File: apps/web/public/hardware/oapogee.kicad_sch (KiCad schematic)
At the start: 44 parts, among them J1 USB4085-GF-A, J2 S2B-PH-K-S, J3 U.FL-R-SMT-1(10), J4 SWD-PADS, J5 U.FL-R-SMT-1(10), SW1 JS102011SCQN, SW2 B3U-1000P, SW3 B3U-1000P, U1 MCP73831, U2 TPS63001, U3 RP2350A, U4 W25Q128JVSIQ, U5 BMP390, U6 ICM-42688-P, U7 ADXL375, U8 SX1262, U9 MAX-M10S, Y1 ABM8-272-T3

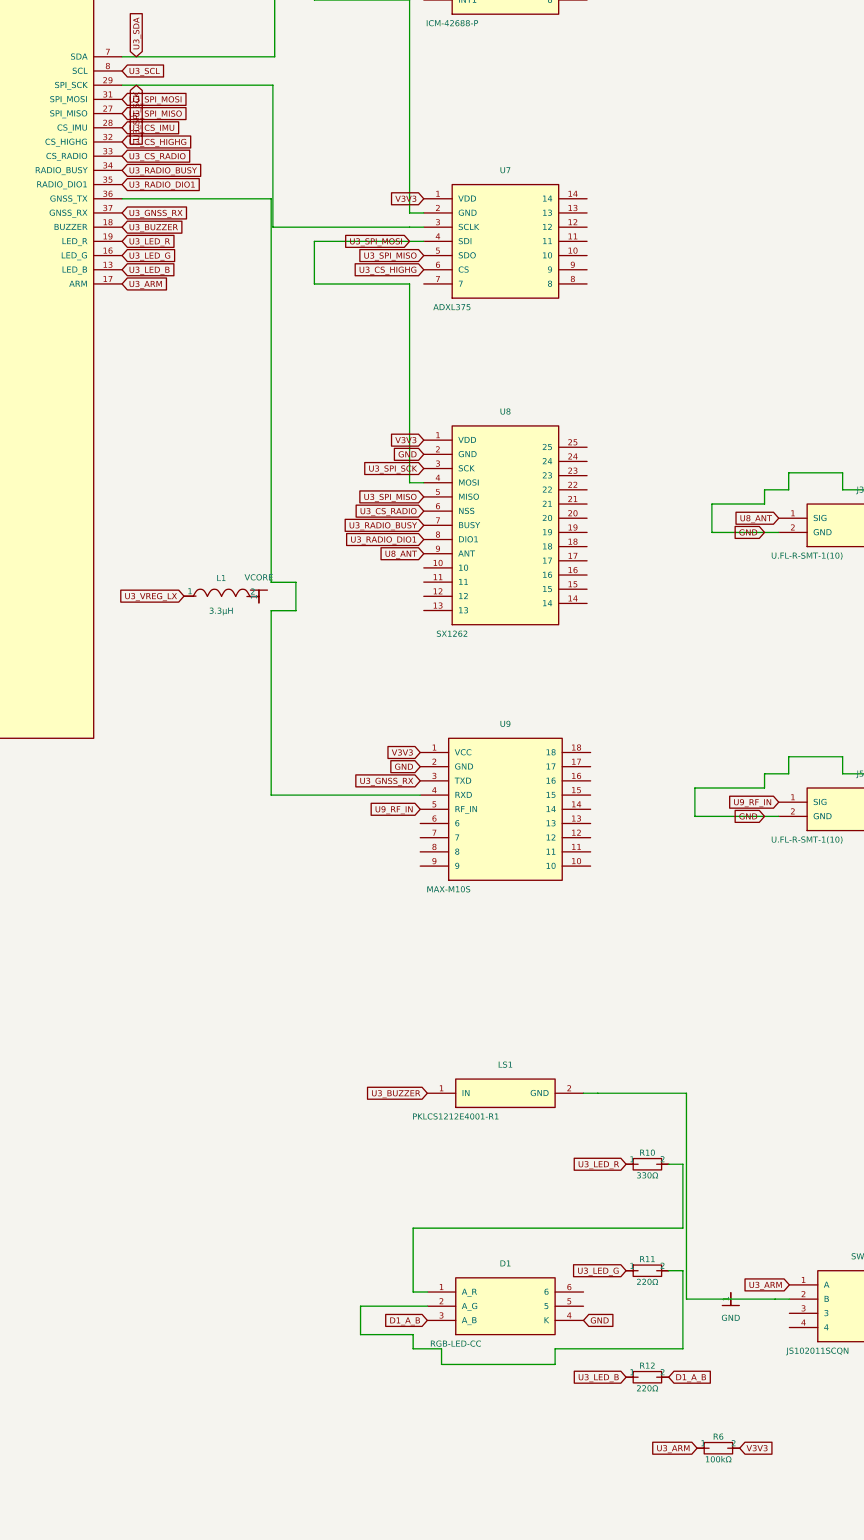
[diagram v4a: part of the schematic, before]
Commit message: Build the radio properly: the real SX1262 pinout, its crystal, its DC-DC
Semtech DS.SX1261-2.W.APP Table 2-1, transcribed for the QFN 4x4 24L and
cross-checked against revision 1.2 from 2019 and revision 2.2 from 2024. The
part had nine of twenty-five pins named. It has all of them now, and the four
supplies, four grounds, exposed pad, reset and DIO2 are wired.

Two parts the datasheet requires that this board did not have:

Y2, a 32 MHz crystal, because the radio has no reference without one. And it
gets no load capacitors, which looks like an omission next to the
microcontroller's crystal ten millimetres away and is not. Section 4.1.3: the
SX1262 "does not require the user to set external foot capacitors on the XTAL",
because it has programmable ones on XTA and XTB that cannot be switched off and
that the state machine sets to 19.7 pF on entering STDBY_XOSC. Adding external
capacitors would detune it.

L3, 15 uH between VREG and DCC_SW, which is what lets the radio use its
switching regulator instead of its linear one. Section 13.1.11 on not fitting
it: "Using only a linear regulator implies that the RX or TX current is almost
doubled." On a payload built around one small cell that is the largest single
number in the power budget.

The board is 92 mm rather than 78. Sixteen more connections in one corner put
the autorouter into a state where it was pushing vias to 0.028 mm from pads and
laying 114 pairs of copper that crossed each other, which is 114 shorts. More
length fixed it: 145 traces, no crossings, and the count of pairs too close for
the cheaper fabricator fell from 82 back to 40.

It is still 28 mm wide. Widening to 30 routed just as well and was wrong: the
sled has to slide into a 32.59 mm tube, so a 30 mm board leaves 1.3 mm a side
for a wall the sled prints at 1.2 mm. The router did not need the width.

What is still open, and it is one thing: the RF front end. The transmit output,
the receive inputs and the PA supply are still unconnected, because bet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
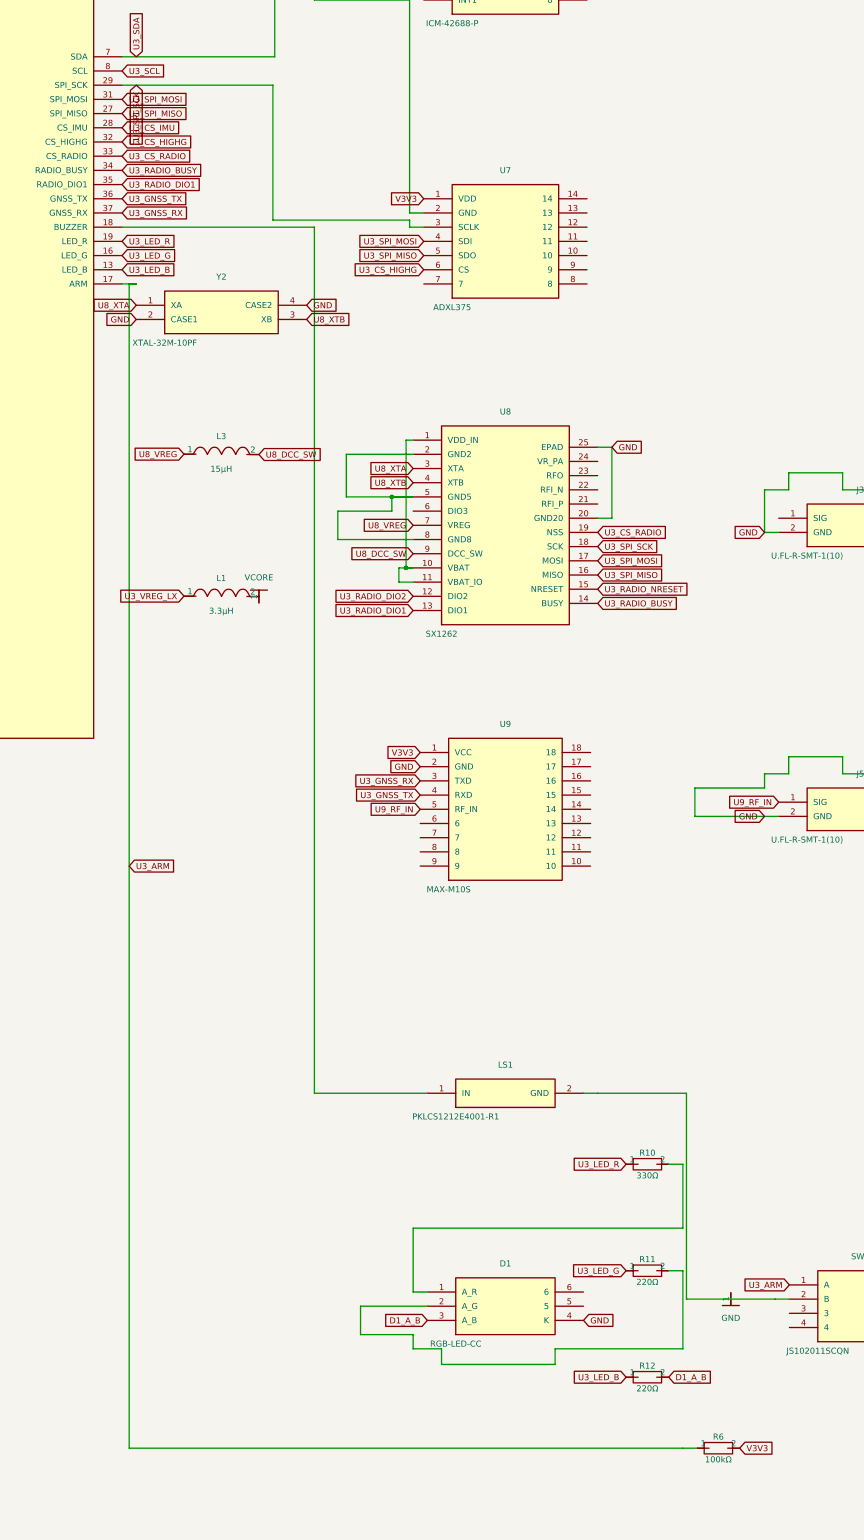
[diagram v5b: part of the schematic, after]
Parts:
- removed GND (x3): GND, symbol Custom:rail_down
- added GND (x3): GND, symbol Custom:rail_down
- added L3: 15µH, symbol Device:inductor_right
- added Y2: XTAL-32M-10PF, symbol Device:U_XTAL-32M-10PF
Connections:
- net GND: now also U8.20 (GND20), U8.25 (EPAD), Y2.2 (CASE1), Y2.4 (CASE2); no longer U8.2 (GND)
- net U3_CS_RADIO: now also U8.19 (NSS); no longer U8.6 (NSS)
- net U3_RADIO_BUSY: now also U8.14 (BUSY); no longer U8.7 (BUSY)
- net U3_RADIO_DIO1: now also U8.13 (DIO1); no longer U8.8 (DIO1)
- net U3_SPI_MISO: now also U8.16 (MISO); no longer U8.5 (MISO)
- net U3_SPI_MOSI: now also U8.17 (MOSI); no longer U8.4 (MOSI)
- net U3_SPI_SCK: now also U8.18 (SCK); no longer U8.3 (SCK)
- net V3V3: no longer U8.1 (VDD)
- net U3_GNSS_TX: now reaches U3.36 (GNSS_TX), U9.4 (RXD)
- net at U8.10 (VBAT): now also U8.1 (VDD_IN), U8.11 (VBAT_IO)
- net U3_RADIO_DIO2: now reaches U8.12 (DIO2)
- net U3_RADIO_NRESET: now reaches U8.15 (NRESET)
- net U3_BUZZER: no longer names the net of LS1.1 (IN), U3.18 (BUZZER)
- net U8_ANT: no longer names the net of J3.1 (SIG)
- net U8_ANT: no longer U8.9 (ANT)
- new net: U8.2 (GND2), U8.5 (GND5), U8.8 (GND8)
- new net U8_DCC_SW: L3.2, U8.9 (DCC_SW)
- new net U8_VREG: L3.1, U8.7 (VREG)
- new net U8_XTA: U8.3 (XTA), Y2.1 (XA)
- new net U8_XTB: U8.4 (XTB), Y2.3 (XB)

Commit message: Transcribe all seven remaining pinouts, and two of them were fatal
Six datasheets read by parallel agents, each verified by a second agent working
from an independently obtained source, usually a different revision or a
different mirror. Every disagreement they found was provenance or figure
numbering. Not one pin assignment was disputed. The seventh, the LED, is handled
below.

Two of the seven guesses this replaces would have produced a dead board:

The barometer had SDA on pin 3, and pin 3 of a BMP390 is VSS. That is the I2C
data line shorted to ground, which takes out the bus rather than just the part.

The IMU had VDD on pin 1, and pin 1 of an ICM-42688-P is AP_SDO, the part's own
data output. A 3.3 V rail connected to an output driver.

Three more were wrong without being fatal. The high-g accelerometer had the SPI
clock on pin 3, which the ADXL375 datasheet says "must be connected to VS or
left open"; its pin 11 is the opposite, ground or open, and a schematic treating
the two reserved pins alike is wrong on one of them. The GNSS receiver had VCC on
pin 1, which is ground, and RF_IN on pin 5, which is pin 11. The slide switch had
a seven pad footprint and the part has three terminals: C&K's recommended land
pattern has three pads and no mounting lands, staggered across two rows rather
than in a line, so the footprint muscle memory draws leaves a lead in mid-air.

The USB connector was the most dangerous. Its two rows run in OPPOSITE
directions, so pins do not pair vertically: column 4 is data plus above data
minus, column 5 is data minus above data plus. Bridging down a column, which is
what the ground and VBUS columns invite you to do, shorts D+ to D-. The correct
connections are two diagonals that cross. All four VBUS and all four ground pins
are now wired, because they are rated collectively and leaving some off does not
lower the rating, it concentrates the current.

Seven capacitors came out of the same reading, each named in a datasheet: two on
the baro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
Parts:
- removed GND (x3): GND, symbol Custom:rail_down
- added C10: 10nF, symbol Device:capacitor_right
- added C11, C6, C7, C8: 100nF, symbol Device:capacitor_right
- added C12: 1uF, symbol Device:capacitor_right
- added C9: 2.2uF, symbol Device:capacitor_right
- added GND (x3): GND, symbol Custom:rail_down
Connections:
- net D1_A_B: now also D1.1 (A_B); no longer D1.3 (A_B)
- net GND: now also D1.2 (K_B), J1.1 (A1), J1.16 (B1), J1.17 (SHELL00), J1.18 (SHELL01), J1.19 (SHELL10), J1.20 (SHELL11), J1.8 (A12), J1.9 (B12), LS1.2 (GND), SW1.1 (T1), U1.2 (VSS), U5.3 (VSS3), U5.5 (SDO), U6.10 (RESV10), U6.11 (RESV11), U6.3 (RESV3), U6.6 (GND), U6.7 (RESV7), U7.11 (RESV11), U8.2 (GND2), U8.5 (GND5), U8.8 (GND8), U9.1 (GND1), C10.2, C11.2, C12.2, C6.2, C7.2, C8.2, C9.2; no longer D1.4 (K), J1.2 (GND), J2.2 (GND), U7.2 (GND), U9.2 (GND), Y2.4 (CASE2)
- net U3_ARM: now also SW1.2 (COM); no longer SW1.1 (A)
- net U3_CS_HIGHG: now also U7.7 (CS); no longer U7.6 (CS)
- net U3_CS_IMU: now also U6.12 (CS); no longer U6.6 (CS)
- net U3_GNSS_RX: now also U9.2 (TXD); no longer U9.3 (TXD)
- net U3_GNSS_TX: now also U9.3 (RXD); no longer U9.4 (RXD)
- net U3_SCL: now also U5.2 (SCL); no longer U5.4 (SCL)
- net U3_SDA: now also U5.4 (SDA); no longer U5.3 (SDA)
- net U3_SPI_MISO: now also U6.1 (SDO), U7.12 (SDO); no longer U6.5 (SDO), U7.5 (SDO)
- net U3_SPI_MOSI: now also U6.14 (SDI), U7.13 (SDI); no longer U6.4 (SDI), U7.4 (SDI)
- net U3_SPI_SCK: now also U6.13 (SCLK), U7.14 (SCLK); no longer U6.3 (SCLK), U7.3 (SCLK)
- net U3_USB_DM: now also J1.12 (B7), J1.5 (A7); no longer J1.4 (DM)
- net U3_USB_DP: now also J1.13 (B6), J1.4 (A6); no longer J1.3 (DP)
- net U9_RF_IN: now also U9.11 (RF_IN); no longer U9.5 (RF_IN)
- net V3V3: now also U5.1 (VDDIO), U5.10 (VDD), U5.6 (CSB), U6.5 (VDDIO), U6.8 (VDD), U9.6 (V_BCKP), U9.7 (V_IO), U9.8 (VCC), C10.1, C11.1, C12.1, C6.1, C7.1, C8.1, C9.1; no longer U7.1 (VDD), U9.1 (VCC)
- net J1_pin2: now reaches U1.4 (VDD)
- net J1_pin2: now also J1.10 (B9), J1.15 (B4), J1.2 (A4), J1.7 (A9); no longer J1.1 (VBUS)
- net J1_pin14: now reaches J1.14 (B5)
- net J1_pin14: now also R2.1
- net J1_pin3: now reaches R1.1
- net J1_pin3: now also J1.3 (A5); no longer J1.5 (CC1)
- net at U9.10 (GND10): now also U9.12 (GND12)
- net D1_A_R: now reaches R10.2
- net D1_A_R: now also D1.3 (A_R); no longer D1.1 (A_R)
- net at R11.2: now also D1.5 (A_G); no longer D1.2 (A_G)
- net at D1.6 (K_G): now also D1.4 (K_R)
- net at R3.2: now also J2.2 (GND); no longer U1.2 (VSS)
- net at U5.8 (VSS8): now also U5.9 (VSS9)
- net J1_CC2: no longer names the net of J1.6 (A8)
- net J1_CC2: no longer R2.1
- new net: U7.2 (GND2), U7.4 (GND4), U7.5 (GND5), Y2.4 (CASE2)
- new net: U7.1 (VDDIO), U7.3 (RESV3), U7.6 (VS)
